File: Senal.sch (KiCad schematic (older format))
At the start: 19 parts, among them P1 GSG-RF-CONN, P2 GSG-RF-CONN, P3 CONN_02X04, P4 CONN_01X01, U1 AD8606, U2 ADG849, U3 AD5933

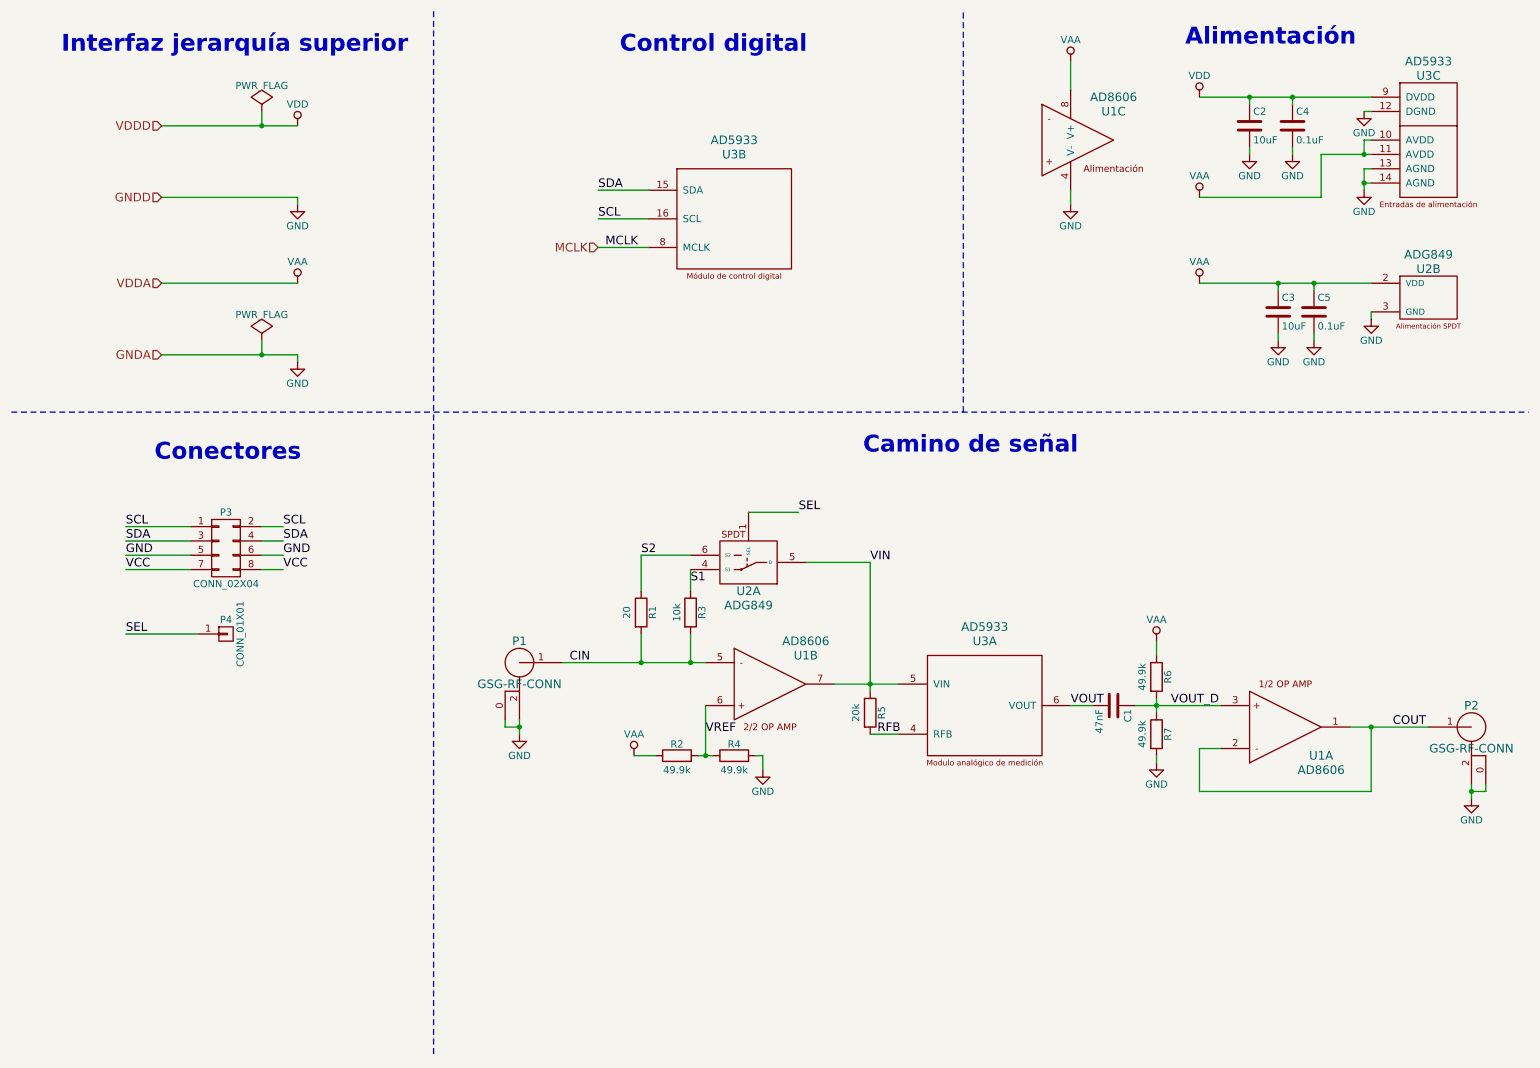
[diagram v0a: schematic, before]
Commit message: Ruteados los conjuntos por separado
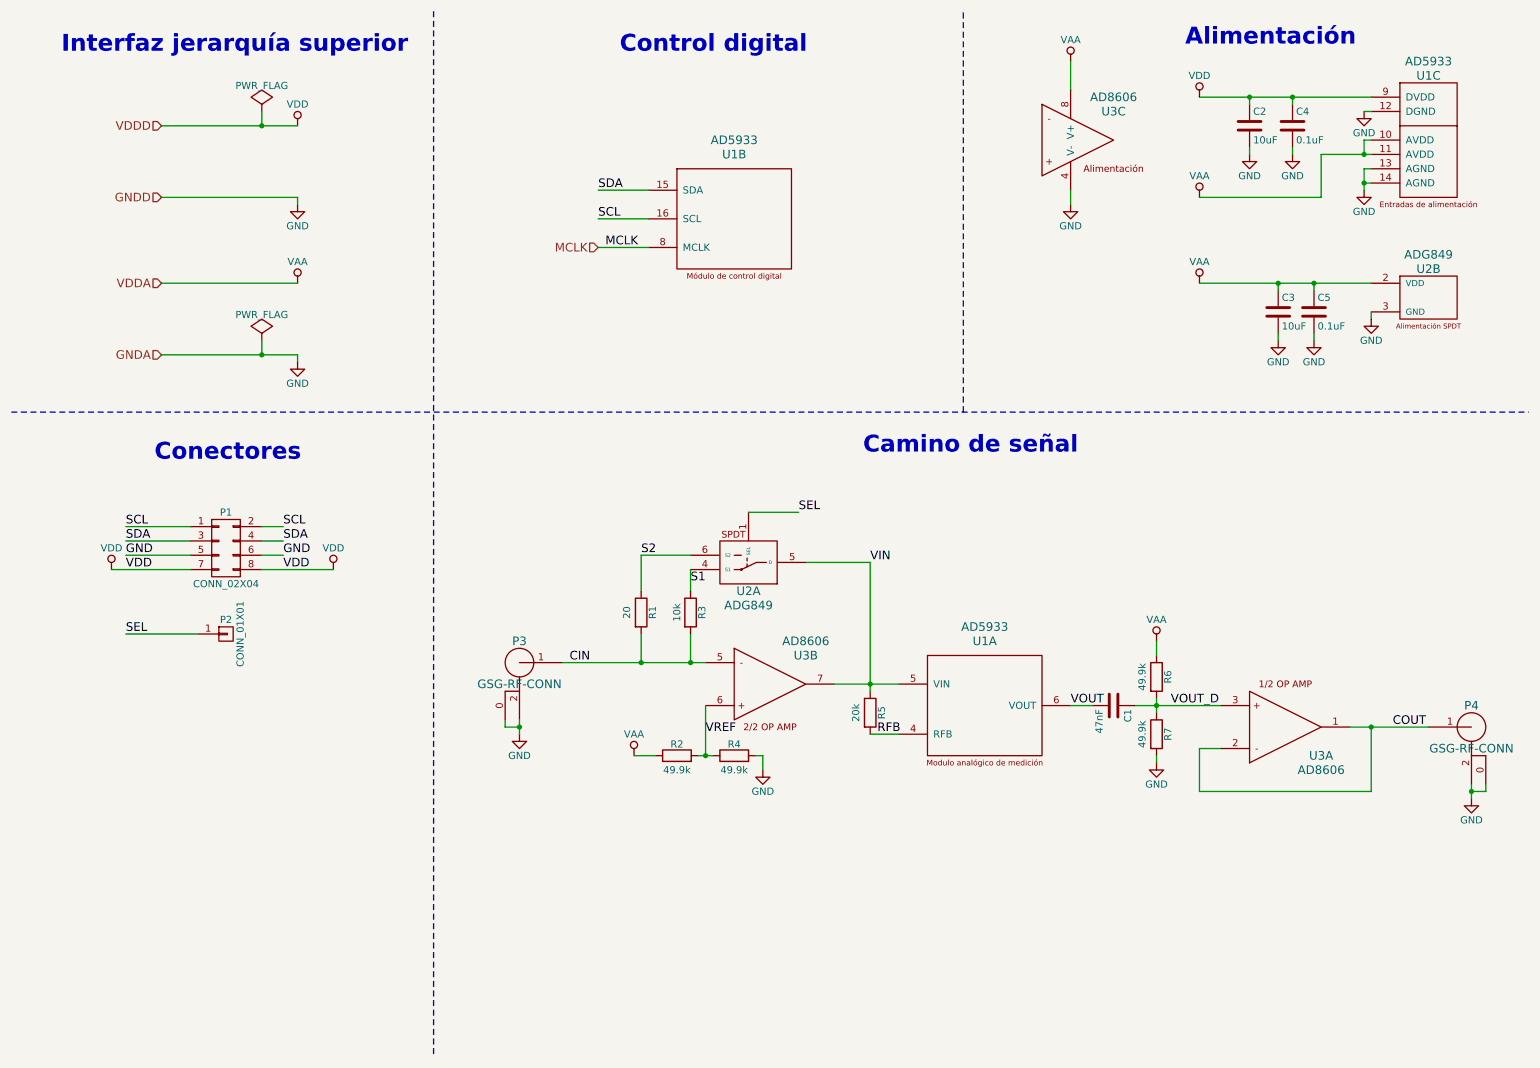
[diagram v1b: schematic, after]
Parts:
- P3: renamed from P1; footprint propios:sma -> SMA_EDGE:SMA_EDGE
- P4: renamed from P2; footprint propios:sma -> SMA_EDGE:SMA_EDGE
- renumbered P3 to P1, P4 to P2, U3 to U1, U1 to U3
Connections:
- net VCC is gone; now on net VDD: P1.7 (P7), P1.8 (P8)
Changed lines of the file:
@@
 MCLK
 $Comp
-L AD5933 U3
+L AD5933 U1
 U 3 1 582F7476
 P 10450 1400
-F 0 "U3" H 10450 1850 60  0000 C CNN
+F 0 "U1" H 10450 1850 60  0000 C CNN
 F 1 "AD5933" H 10450 1950 60  0000 C CNN
 F 2 "Housings_SSOP:SSOP-16_5.3x6.2mm_Pitch0.65mm" H 10450 1400 60  0001 C CNN
@@
 $EndComp
 $Comp
-L AD5933 U3
+L AD5933 U1
 U 2 1 582F78D1
 P 5600 1950
-F 0 "U3" H 5600 2400 60  0000 C CNN
+F 0 "U1" H 5600 2400 60  0000 C CNN
 F 1 "AD5933" H 5600 2500 60  0000 C CNN
 F 2 "Housings_SSOP:SSOP-16_5.3x6.2mm_Pitch0.65mm" H 5600 1950 60  0001 C CNN
@@
 $EndComp
 $Comp
-L AD5933 U3
+L AD5933 U1
 U 1 1 582F791E
 P 7350 5350
-F 0 "U3" H 7350 5800 60  0000 C CNN
+F 0 "U1" H 7350 5800 60  0000 C CNN
 F 1 "AD5933" H 7350 5900 60  0000 C CNN
 F 2 "Housings_SSOP:SSOP-16_5.3x6.2mm_Pitch0.65mm" H 7350 5350 60  0001 C CNN
@@
 $EndComp
 $Comp
-L AD8606 U1
+L AD8606 U3
 U 3 1 582F7A24
 P 8000 1400
-F 0 "U1" H 8250 1600 60  0000 C CNN
+F 0 "U3" H 8250 1600 60  0000 C CNN
 F 1 "AD8606" H 8250 1700 60  0000 C CNN
 F 2 "Housings_SSOP:MSOP-8_3x3mm_Pitch0.65mm" H 8000 1400 60  0001 C CNN
@@
 $EndComp
 $Comp
-L AD8606 U1
+L AD8606 U3
 U 1 1 582F8028
 P 9450 5500
-F 0 "U1" H 9700 5700 60  0000 C CNN
+F 0 "U3" H 9700 5700 60  0000 C CNN
 F 1 "AD8606" H 9700 5800 60  0000 C CNN
 F 2 "Housings_SSOP:MSOP-8_3x3mm_Pitch0.65mm" H 9450 5500 60  0001 C CNN
@@
 $EndComp
 $Comp
-L AD8606 U1
+L AD8606 U3
 U 2 1 582F8067
 P 5850 5200
-F 0 "U1" H 6100 5400 60  0000 C CNN
+F 0 "U3" H 6100 5400 60  0000 C CNN
 F 1 "AD8606" H 6100 5500 60  0000 C CNN
 F 2 "Housings_SSOP:MSOP-8_3x3mm_Pitch0.65mm" H 5850 5200 60  0001 C CNN
@@
 $EndComp
 $Comp
-L GSG-RF-CONN P2
+L GSG-RF-CONN P4
 U 1 1 582FC1E0
 P 10750 5500
-F 0 "P2" H 10750 5650 60  0000 C CNN
+F 0 "P4" H 10750 5650 60  0000 C CNN
 F 1 "GSG-RF-CONN" H 10750 5350 60  0000 C CNN
-F 2 "propios:sma" H 10750 5500 60  0001 C CNN
+F 2 "SMA_EDGE:SMA_EDGE" H 10750 5500 60  0001 C CNN
 F 3 "" H 10750 5500 60  0000 C CNN
 F 4 "WM5534-ND" H 10750 5500 60  0001 C CNN "Digikey#"
@@
 $EndComp
 $Comp
-L GSG-RF-CONN P1
+L GSG-RF-CONN P3
 U 1 1 582FCD4C
 P 4100 5050
-F 0 "P1" H 4100 5200 60  0000 C CNN
+F 0 "P3" H 4100 5200 60  0000 C CNN
 F 1 "GSG-RF-CONN" H 4100 4900 60  0000 C CNN
-F 2 "propios:sma" H 4100 5050 60  0001 C CNN
+F 2 "SMA_EDGE:SMA_EDGE" H 4100 5050 60  0001 C CNN
 F 3 "" H 4100 5050 60  0000 C CNN
 	1    4100 5050
@@
 Camino de señal
 $Comp
-L CONN_02X04 P3
+L CONN_02X04 P1
 U 1 1 58375283
 P 2050 4250
-F 0 "P3" H 2050 4500 50  0000 C CNN
+F 0 "P1" H 2050 4500 50  0000 C CNN
 F 1 "CONN_02X04" H 2050 4000 50  0000 C CNN
 F 2 "Pin_Headers:Pin_Header_Straight_2x04" H 2050 3050 50  0001 C CNN
@@
 	1350 4300 1800 4300
 Wire Wire Line
-	1350 4400 1800 4400
+	1250 4400 1800 4400
 Wire Wire Line
 	2300 4300 2450 4300
 Wire Wire Line
-	2300 4400 2450 4400
+	2300 4400 2800 4400
 Text Label 1350 4100 0    60   ~ 0
 SCL
@@
 Text Label 2450 4300 0    60   ~ 0
 GND
-Text Label 1350 4400 0    60   ~ 0
-VCC
-Text Label 2450 4400 0    60   ~ 0
-VCC
-$Comp
-L CONN_01X01 P4
+$Comp
+L CONN_01X01 P2
 U 1 1 5837592F
 P 2050 4850
-F 0 "P4" H 2050 4950 50  0000 C CNN
+F 0 "P2" H 2050 4950 50  0000 C CNN
 F 1 "CONN_01X01" V 2150 4850 50  0000 C CNN
 F 2 "Pin_Headers:Pin_Header_Straight_1x01" H 2050 4850 50  0001 C CNN
@@
 Text Label 5295 4497 0    60   ~ 0
 S1
+Text Label 2450 4400 0    60   ~ 0
+VDD
+Text Label 1350 4400 0    60   ~ 0
+VDD
+$Comp
+L VDD #PWR?
+U 1 1 584B3CB6
+P 2800 4400
+F 0 "#PWR?" H 2800 4250 50  0001 C CNN
+F 1 "VDD" H 2800 4550 50  0000 C CNN
+F 2 "" H 2800 4400 50  0000 C CNN
+F 3 "" H 2800 4400 50  0000 C CNN
+	1    2800 4400
+	1    0    0    -1
+$EndComp
+$Comp
+L VDD #PWR?
+U 1 1 584B3CFA
+P 1250 4400
+F 0 "#PWR?" H 1250 4250 50  0001 C CNN
+F 1 "VDD" H 1250 4550 50  0000 C CNN
+F 2 "" H 1250 4400 50  0000 C CNN
+F 3 "" H 1250 4400 50  0000 C CNN
+	1    1250 4400
+	1    0    0    -1
+$EndComp
 $EndSCHEMATC

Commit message: Se quitaron librerias sobrantes y se actualizaron los footprints a kicad_mod
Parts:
- P3: Digikey# (none) -> WM5534-ND
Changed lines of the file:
@@
 F 2 "SMA_EDGE:SMA_EDGE" H 4100 5050 60  0001 C CNN
 F 3 "" H 4100 5050 60  0000 C CNN
+F 4 "WM5534-ND" H 4100 5050 60  0001 C CNN "Digikey#"
 	1    4100 5050
 	1    0    0    -1
@@
 VDD
 $Comp
-L VDD #PWR?
+L VDD #PWR025
 U 1 1 584B3CB6
 P 2800 4400
-F 0 "#PWR?" H 2800 4250 50  0001 C CNN
+F 0 "#PWR025" H 2800 4250 50  0001 C CNN
 F 1 "VDD" H 2800 4550 50  0000 C CNN
 F 2 "" H 2800 4400 50  0000 C CNN
@@
 $EndComp
 $Comp
-L VDD #PWR?
+L VDD #PWR026
 U 1 1 584B3CFA
 P 1250 4400
-F 0 "#PWR?" H 1250 4250 50  0001 C CNN
+F 0 "#PWR026" H 1250 4250 50  0001 C CNN
 F 1 "VDD" H 1250 4550 50  0000 C CNN
 F 2 "" H 1250 4400 50  0000 C CNN

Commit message: Correcciones sugeridas por la 2da revision efectuada por D. Brengi
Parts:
- C2, C3, C4, C5: Digikey# (none) -> 478-1215-1-ND
- U1: Digikey# (none) -> AD5933YRSZ-REEL7CT-ND
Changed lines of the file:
@@
 LIBS:power
 LIBS:device
-LIBS:transistors
 LIBS:conn
-LIBS:linear
-LIBS:regul
-LIBS:74xx
-LIBS:cmos4000
-LIBS:adc-dac
-LIBS:memory
-LIBS:xilinx
-LIBS:microcontrollers
-LIBS:dsp
-LIBS:microchip
-LIBS:analog_switches
-LIBS:motorola
-LIBS:texas
-LIBS:intel
-LIBS:audio
-LIBS:interface
-LIBS:digital-audio
-LIBS:philips
-LIBS:display
-LIBS:cypress
-LIBS:siliconi
-LIBS:opto
-LIBS:atmel
-LIBS:contrib
-LIBS:valves
 LIBS:PMOD_IA
 LIBS:SMA
-LIBS:sma2
 LIBS:proyectoDCI-cache
 EELAYER 25 0
@@
 Comment1 "Autor: LAROSA, F."
 Comment2 "Revisor: GIGLIOTTI, E."
-Comment3 ""
-Comment4 ""
+Comment3 "Licencia: BSD"
+Comment4 "Asignatura: Diseño de Circuitos Impresos"
 $EndDescr
 Text HLabel 1600 1300 0    60   Input ~ 0
@@
 F 2 "Housings_SSOP:SSOP-16_5.3x6.2mm_Pitch0.65mm" H 10450 1400 60  0001 C CNN
 F 3 "" H 10450 1400 60  0001 C CNN
+F 4 "AD5933YRSZ-REEL7CT-ND" H 10450 1400 60  0001 C CNN "Digikey#"
 	3    10450 1400
 	1    0    0    -1
@@
 F 2 "Capacitors_SMD:C_0603" H 9238 1150 50  0001 C CNN
 F 3 "" H 9200 1300 50  0000 C CNN
+F 4 "478-1215-1-ND" H 9200 1300 60  0001 C CNN "Digikey#"
 	1    9200 1300
 	1    0    0    -1
@@
 F 2 "Capacitors_SMD:C_0603" H 9538 1150 50  0001 C CNN
 F 3 "" H 9500 1300 50  0000 C CNN
+F 4 "478-1215-1-ND" H 9500 1300 60  0001 C CNN "Digikey#"
 	1    9500 1300
 	1    0    0    -1
@@
 F 2 "Capacitors_SMD:C_0603" H 9438 2450 50  0001 C CNN
 F 3 "" H 9400 2600 50  0000 C CNN
+F 4 "478-1215-1-ND" H 9400 2600 60  0001 C CNN "Digikey#"
 	1    9400 2600
 	1    0    0    -1
@@
 F 2 "Capacitors_SMD:C_0603" H 9688 2450 50  0001 C CNN
 F 3 "" H 9650 2600 50  0000 C CNN
+F 4 "478-1215-1-ND" H 9650 2600 60  0001 C CNN "Digikey#"
 	1    9650 2600
 	1    0    0    -1
